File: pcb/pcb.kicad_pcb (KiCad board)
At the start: 2 copper layers, 104.1 x 53.3 mm, 22 parts, among them J1 processor_right, J2 processor_left, J3 GSM, J4 charger, J5 sensors, J6 BME_280, J7 debug_pwr_jumper

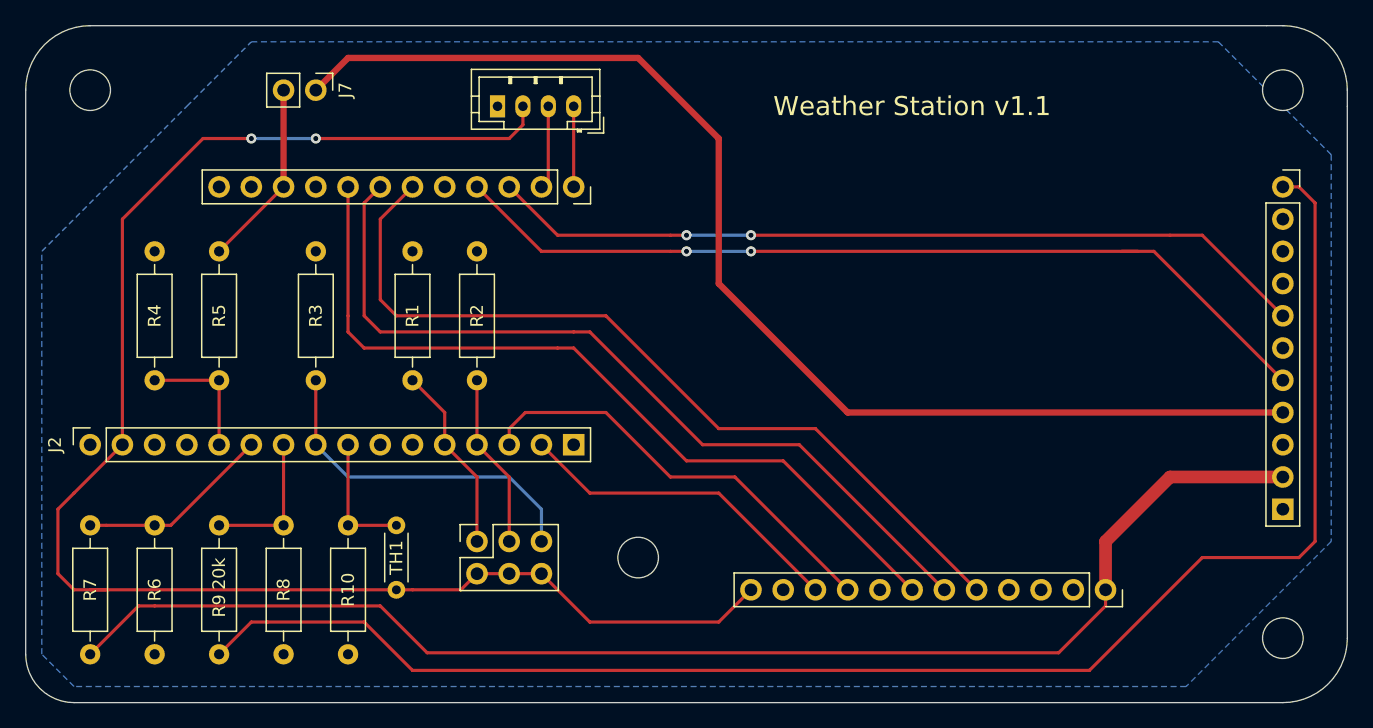
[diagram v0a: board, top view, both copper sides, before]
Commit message: Doubling line thickness
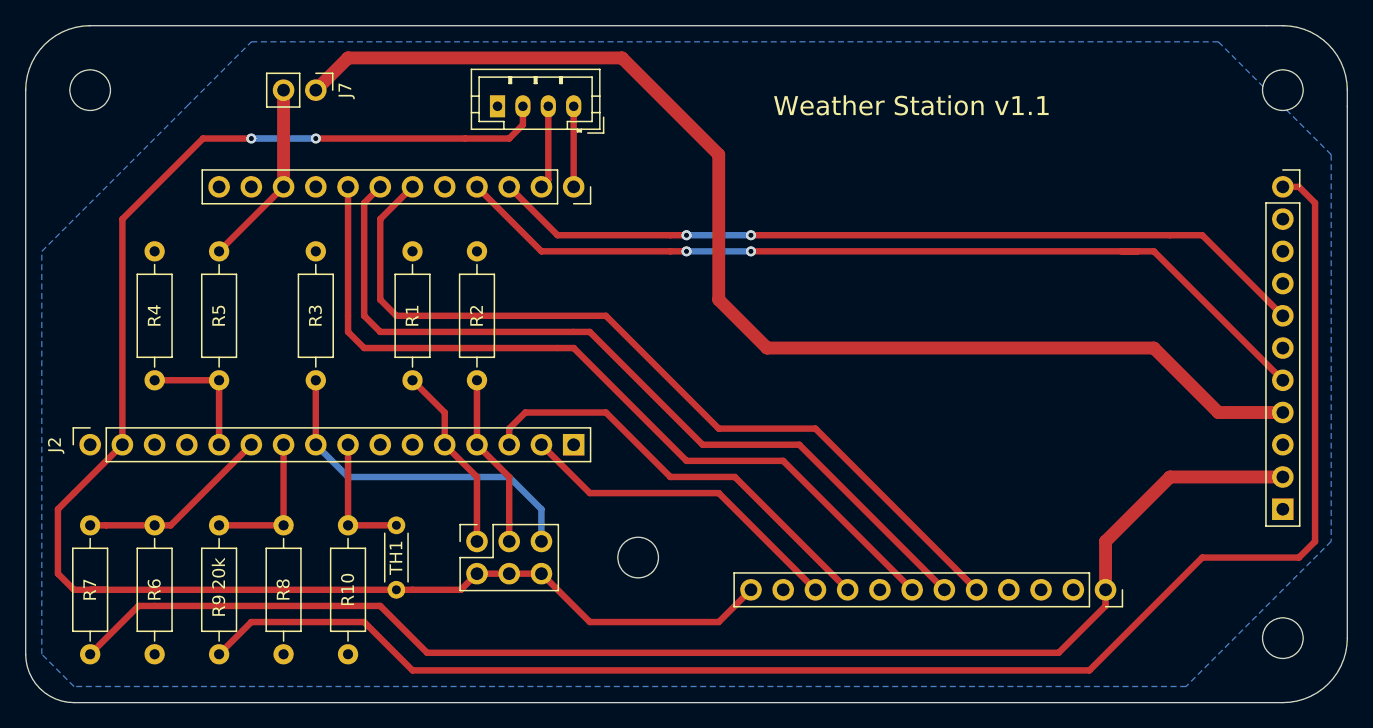
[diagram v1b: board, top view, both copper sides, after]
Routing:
- net PROC_PWR: track 14.2 -> 14.8 mm

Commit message: Fixes.
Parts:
- R9: value 20k -> 22k
- moved R6 5.08 mm to (119.4, 128.3)
- moved R7 5.08 mm to (124.5, 138.4)
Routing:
- net +BATT: track 105.8 -> 100.7 mm
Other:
- board text removed: "20k"
